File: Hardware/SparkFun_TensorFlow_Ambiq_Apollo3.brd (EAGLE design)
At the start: 40 x 40 mm, 100 parts, among them J5 CORTEX_DEBUG, J6 CAMERA-OV7670, U2 LIS2DH12, U3 1.8V, U5 ARTEMIS_MODULESMD, Y2 32.768kHz

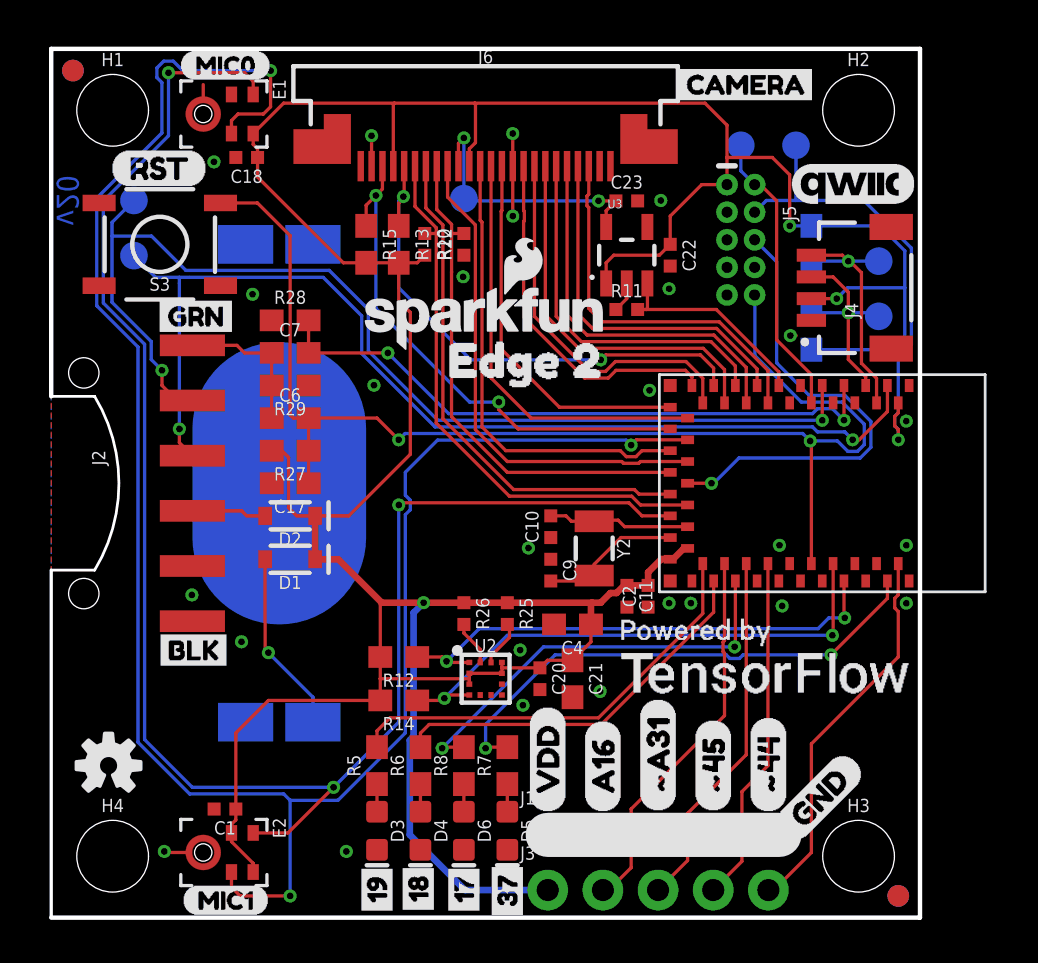
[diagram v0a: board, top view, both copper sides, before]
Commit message: Invert JTAG connector
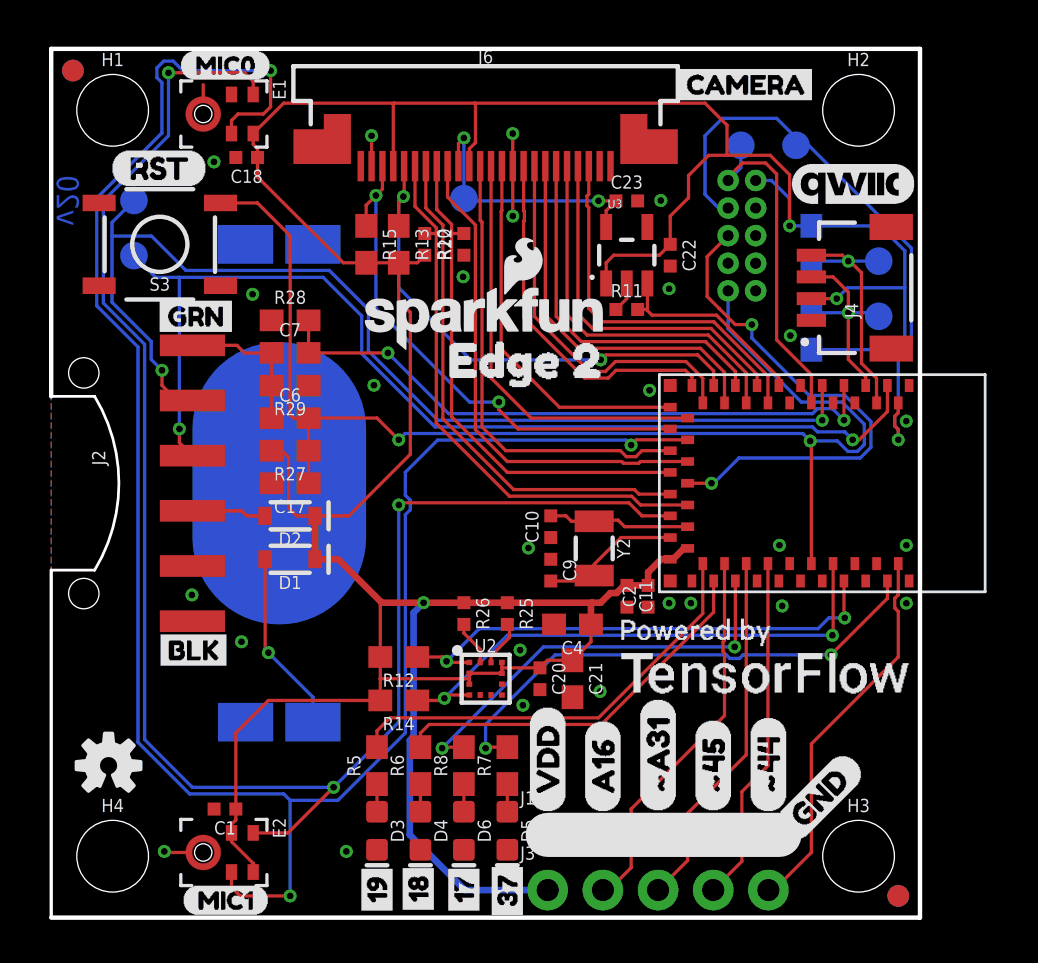
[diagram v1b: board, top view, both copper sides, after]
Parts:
- J5: device SparkFun-Connectors:2X5-PTH-1.27MM-NO_SILK -> SparkFun-Connectors:2X5-PTH-1.27MM
- moved J5 0.20 mm to (31.8, 31.4), flipped to the bottom
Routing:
- net SWDCK: track 21.9 -> 27.6 mm
- net VDD: track 167.0 -> 170.0 mm
- net SWDIO: track 13.4 -> 15.9 mm
- net ~AD33/SWO: track 21.9 -> 23.8 mm, vias 1 -> 2
- net AMBIQ_!RST: track 58.4 -> 59.0 mm

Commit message: Reroute camera interface to match himax spec
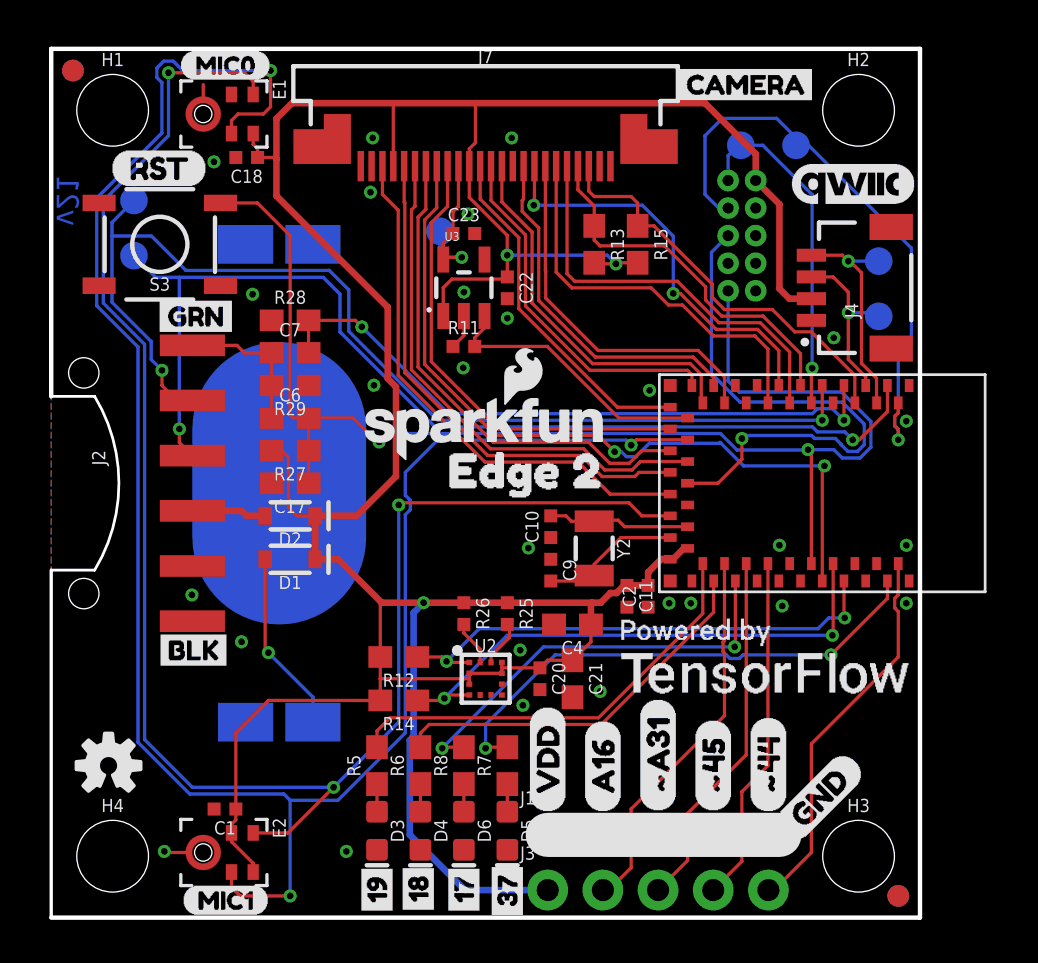
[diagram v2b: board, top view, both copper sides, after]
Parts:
- removed R10, R22: 10k, SparkFun-Resistors:0402-TIGHT
- removed R23, R24: 4.7k, SparkFun-Resistors:0603
- J7: value CAMERA-OV7670 -> CAMERA-HIMAX
- moved R15 12.5 mm to (27.0, 31.0)
- moved R13 9.00 mm to (25.0, 31.0)
- moved R11 7.69 mm to (19.0, 26.3)
- moved C22 7.65 mm to (21.0, 29.0)
- moved C23 7.65 mm to (19.0, 31.5)
- moved U3 7.65 mm to (19.0, 29.0)
- moved LOGO1 5.08 mm to (20.0, 22.5)
- moved U$15 5.08 mm to (16.9, 20.6)
- moved TP7 1.86 mm to (17.9, 31.6)
- renumbered J6 to J7
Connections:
- net CAMERA_Y4 renamed CAMERA_INT
- removed net CAMERA_HREF: J7.9, U5.~AD13
- removed net CAMERA_PWDN: J7.8, R22.2, U5.D15
- removed net CAMERA_RESET: J7.6, R10.1, U5.~AD11
- removed net CAMERA_XCLK: J7.13, U5.~AD32
- removed net CAMERA_Y0: J7.19, U5.~D22
- removed net CAMERA_Y1: J7.21, U5.~D4
- removed net CAMERA_Y2: J7.22, U5.~AD35
- removed net CAMERA_Y3: J7.20, U5.~D24
- removed net CAMERA_Y5: J7.16, U5.~D28
- removed net CAMERA_Y6: J7.14, U5.~D6
- removed net CAMERA_Y7: J7.12, U5.~D26
- new net CAMERA_D0: J7.14, U5.D14
- new net CAMERA_D1: J7.3, U5.AD34
- new net CAMERA_D2: J7.9, U5.~D25
- new net CAMERA_D3: J7.5, U5.D15
- new net CAMERA_D4: J7.12, U5.~D6
- new net CAMERA_D5: J7.20, U5.~D5
- new net CAMERA_D6: J7.19, U5.~AD35
- new net CAMERA_D7: J7.13, U5.~D28
- new net CAMERA_HSYNC: J7.16, U5.~D27
- new net CAMERA_MCLK: J7.8, U5.D0
- new net CAMERA_TRIG: J7.7, U5.~D26
- net CAMERA_DVDD_EN: now also U5.~AD32; no longer U5.D7
- net CAMERA_I2C_SCL: now also J7.21, U5.D8; no longer J7.5, U5.~D27
- net CAMERA_I2C_SDA: now also J7.22, U5.D9; no longer J7.3, U5.~D25
- net CAMERA_PCLK: now also U5.D7; no longer U5.D14
- net CAMERA_VSYNC: now also J7.6, U5.~AD13; no longer J7.7, U5.AD34
- net GND: no longer R22.1
- net QWIIC_SCL: no longer R24.1
- net QWIIC_SDA: no longer R23.1
- net VDD: no longer R10.2, R23.2, R24.2
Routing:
- net CAMERA_MCLK: track 0.00 -> 35.6 mm, vias 0 -> 2
- net CAMERA_RESET: track 25.9 -> 0.00 mm
- net CAMERA_D1: track 0.00 -> 24.7 mm
- net CAMERA_D3: track 0.00 -> 23.8 mm
- net CAMERA_PWDN: track 23.5 -> 0.00 mm
- net CAMERA_HREF: track 23.1 -> 0.00 mm
- net CAMERA_TRIG: track 0.00 -> 23.1 mm
- net CAMERA_D2: track 0.00 -> 21.6 mm
- net CAMERA_Y7: track 21.4 -> 0.00 mm
- net CAMERA_XCLK: track 19.6 -> 0.00 mm
- net CAMERA_D5: track 0.00 -> 19.0 mm
- net CAMERA_D6: track 0.00 -> 18.6 mm
- net CAMERA_Y3: track 17.6 -> 0.00 mm
- net CAMERA_Y2: track 17.4 -> 0.00 mm
- net CAMERA_D0: track 0.00 -> 17.4 mm
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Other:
- board text added: "v21"
- board text removed: "v20"

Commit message: Move MCLK to PWM pin.
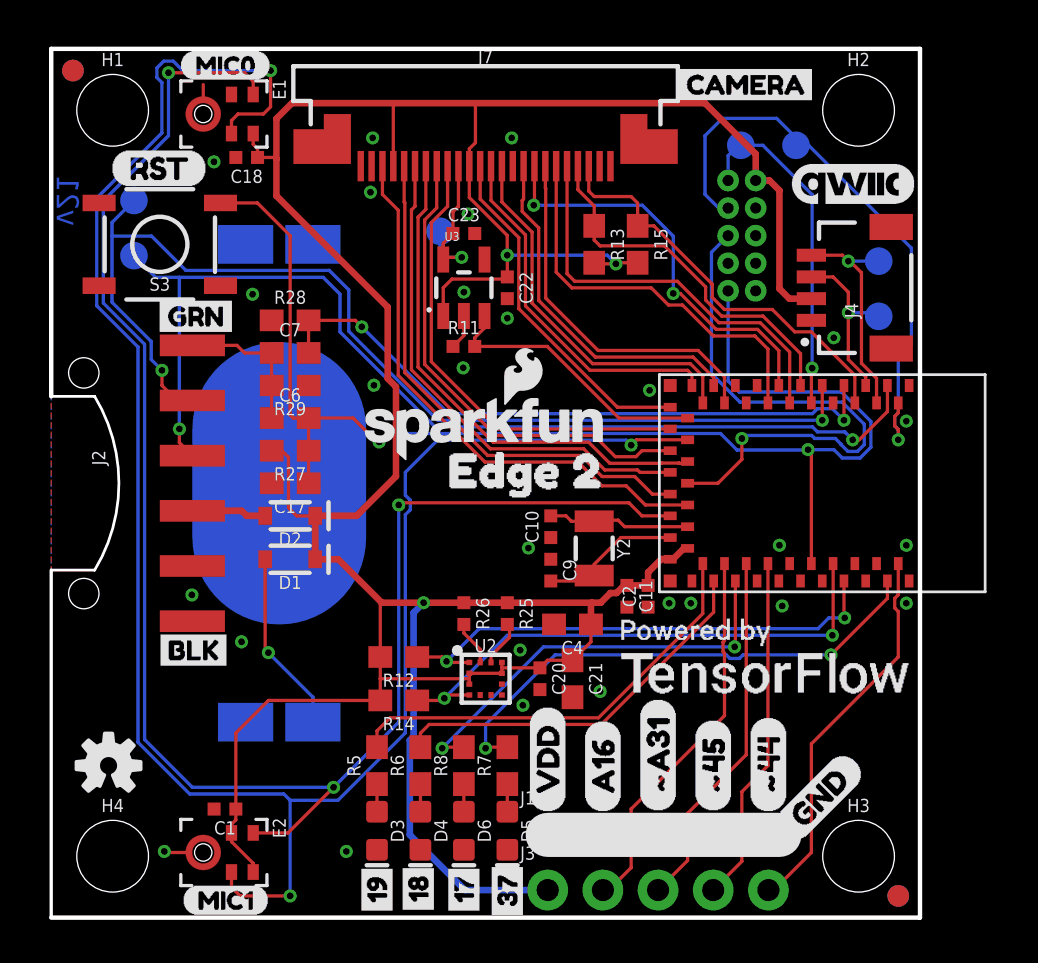
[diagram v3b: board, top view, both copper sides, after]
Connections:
- net CAMERA_D1: now also U5.~AD11; no longer U5.AD34
- net CAMERA_D3: now also U5.AD34; no longer U5.D15
- net CAMERA_MCLK: now also U5.~D26; no longer U5.D0
- net CAMERA_TRIG: now also U5.~AD13; no longer U5.~D26
- net CAMERA_VSYNC: now also U5.D15; no longer U5.~AD13
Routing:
- net CAMERA_MCLK: track 35.6 -> 22.5 mm, vias 2 -> 0
- net CAMERA_D1: track 24.7 -> 25.7 mm
- net CAMERA_VSYNC: track 24.2 -> 23.3 mm
- net CAMERA_TRIG: track 23.1 -> 23.7 mm

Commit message: Move mics to 2cm spacing. Re-wire camera connection.
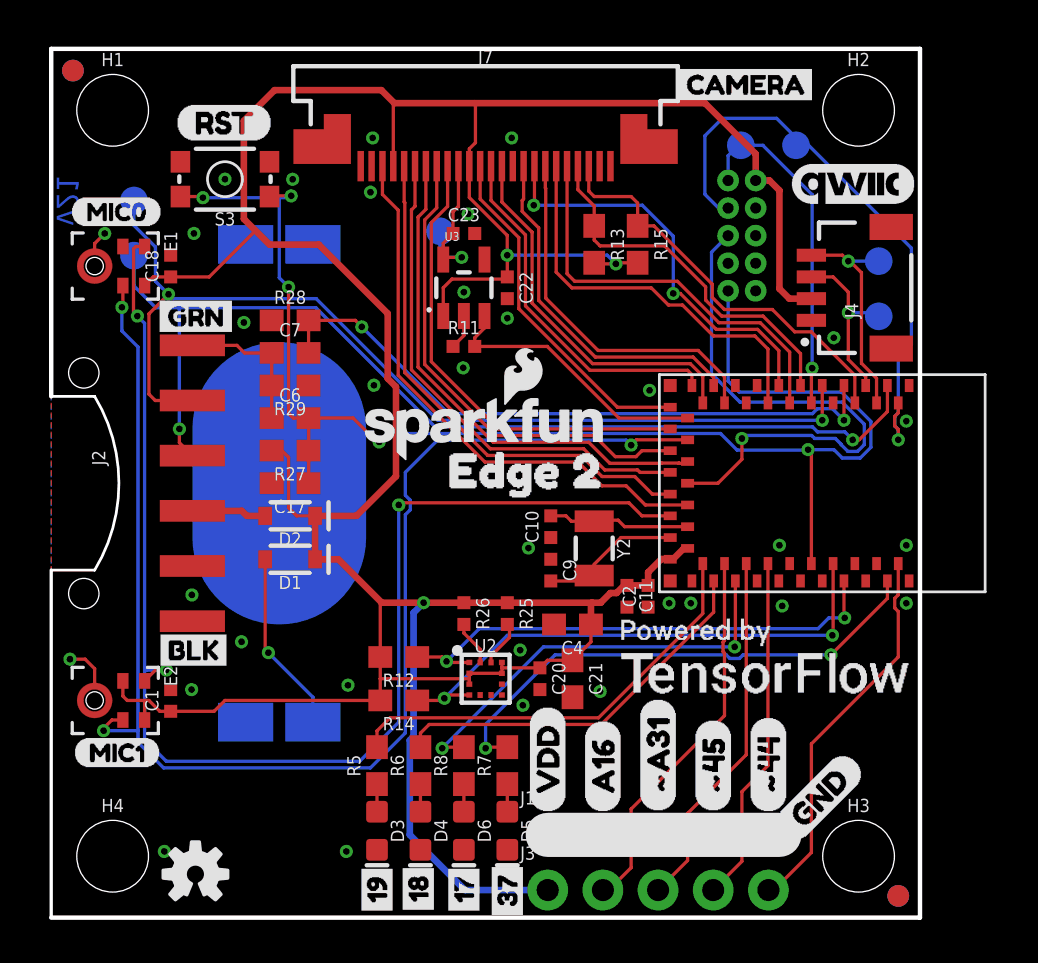
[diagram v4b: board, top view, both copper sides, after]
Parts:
- S3: device SparkFun-Switches:TACTILE_SWITCH_SMD_5.2MM -> SparkFun-Switches:TACTILE_SWITCH_SMD_4.6X2.8MM
- moved E1 8.60 mm to (3.00, 30.0)
- moved E2 8.60 mm to (3.00, 10.0)
- moved U$8 8.44 mm to (1.00, 7.60)
- moved U$1 8.41 mm to (0.90, 32.5)
- moved LOGO2 6.40 mm to (6.64, 2.00)
- moved C18 6.10 mm to (5.50, 30.0), turned to 90 degrees
- moved C1 5.59 mm to (5.50, 10.0), turned to 90 degrees
- moved S3 4.24 mm to (8.00, 34.0)
- moved U$27 3.66 mm to (5.70, 36.6)
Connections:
- net AMBIQ_!RST: now also S3.4
- net GND: now also S3.2
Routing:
- net MIC_CLK: track 91.7 -> 63.6 mm
- net MIC_DATA: track 78.6 -> 61.3 mm
- net VDD: track 156.8 -> 164.6 mm
- net UART-TX: track 50.5 -> 46.2 mm
- net AMBIQ_!RST: track 61.2 -> 65.5 mm, vias 2 -> 5
- net UART-RX: track 49.4 -> 47.8 mm
- net GND: track 12.0 -> 13.3 mm, vias 27 -> 33
